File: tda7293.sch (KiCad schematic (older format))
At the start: 56 parts, among them J1 Screw_Terminal_01x04, J2 Screw_Terminal_01x04, J3 Screw_Terminal_01x02, J4 Screw_Terminal_01x03, Q1 BSS84, Q2 2N7002, U1 TDA7293, U2 TDA7293, U3 PC817, U4 MCP1792

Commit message: C substitutions, status LEDs, layout polishing
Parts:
- removed C1, C7: 22u, Capacitors_SMD:CP_Elec_6.3x7.7, symbol Device:CP
- removed C11, C5: 22u, Capacitors_ThroughHole:CP_Radial_D5.0mm_P2.00mm, symbol Device:CP
- added C1, C11, C24, C25, C5, C7: 10u, Capacitors_SMD:C_1206, symbol Device:C
- added D2, D3, D4: LED, LEDs:LED_0805, symbol Device:LED
- added R14: 1k, Resistors_SMD:R_0805, symbol Device:R
- added R15, R16: 10k, Resistors_SMD:R_0805, symbol Device:R
- C10, C4: footprint Capacitors_SMD:CP_Elec_6.3x7.7 -> Capacitors_ThroughHole:CP_Radial_D8.0mm_P3.50mm
- C2, C8: value 22u -> 22u NP; footprint Capacitors_ThroughHole:CP_Radial_D5.0mm_P2.00mm -> Capacitors_ThroughHole:CP_Radial_D8.0mm_P3.50mm; symbol Device:CP -> Device:C
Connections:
- wire segments 200 -> 229
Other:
- note added: "alt MCP1799"
- moved on the sheet: C10, C14, C15, C16, C17, C18, C19, C20, C21, C22, C23, C3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

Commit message: polishing, plotted output, added README
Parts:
- removed JP3: Jumper_NO_Small, Pin_Headers:Pin_Header_Straight_1x02_Pitch2.00mm, symbol Device:Jumper_NO_Small
- added R17, R18: 27k, Resistors_SMD:R_0805, symbol Device:R
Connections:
- wire segments 229 -> 231
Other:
- note added: "alt footprints\nfor MLCC or\nelectrolytic"
- note removed: "Alt Footprints\nfor 22u/50V\nelectrolytics"
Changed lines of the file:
@@
 	-1   0    0    1
 $EndComp
-Text Label 2500 3200 0    50   ~ 0
-5V
 $Comp
 L Device:R R11
@@
 $EndComp
 Wire Wire Line
-	2750 3800 2750 3850
-Wire Wire Line
 	2750 4000 2850 4000
 $Comp
@@
 Connection ~ 2250 7100
 Wire Wire Line
-	3000 6100 3800 6100
+	3000 6100 3300 6100
 Connection ~ 3000 6100
 Wire Wire Line
-	3000 6600 3800 6600
+	3000 6600 3300 6600
 $Comp
 L wbt-device:TDA7293 U1
@@
 Wire Wire Line
 	8100 2200 8300 2200
-Text Notes 5200 1450 0    50   ~ 0
-Alt Footprints\nfor 22u/50V\nelectrolytics
 Wire Wire Line
 	9200 2100 9200 2200
@@
 	9200 4350 9200 4500
 Connection ~ 8300 4500
-Text Notes 8250 3850 0    50   ~ 0
+Text Notes 8950 1950 0    50   ~ 0
 Close jumpers\nfor TDA7294
 Wire Wire Line
@@
 Wire Wire Line
 	6350 4200 6350 4300
-$Comp
-L Device:Jumper_NO_Small JP3
-U 1 1 61F9C8CB
-P 2250 3000
-F 0 "JP3" H 2250 2815 50  0000 C CNN
-F 1 "Jumper_NO_Small" H 2250 2906 50  0000 C CNN
-F 2 "Pin_Headers:Pin_Header_Straight_1x02_Pitch2.00mm" H 2250 3000 50  0001 C CNN
-F 3 "~" H 2250 3000 50  0001 C CNN
-	1    2250 3000
-	-1   0    0    1
-$EndComp
 Text Notes 3100 3600 0    50   ~ 0
 or AO3401 etc
-Wire Wire Line
-	2350 3000 2850 3000
-Wire Wire Line
-	2150 3000 1800 3000
-Text Label 1850 3000 0    50   ~ 0
-VCC
 Wire Wire Line
 	2000 4650 2050 4650
@@
 	2050 4000 2050 3950
 Wire Wire Line
-	2750 3850 2850 3850
-Wire Wire Line
-	2850 3850 2850 3000
-Connection ~ 2750 3850
-Wire Wire Line
-	2750 3850 2750 4000
-Wire Wire Line
 	2050 3650 2050 3200
 Wire Wire Line
@@
 Wire Wire Line
 	1300 6550 1300 6600
+Text Label 2500 3200 0    50   ~ 0
+5V
+Wire Wire Line
+	2750 3800 2750 4000
+Text Notes 8100 2000 0    50   ~ 0
+alt footprints\nfor MLCC or\nelectrolytic
+$Comp
+L Device:R R17
+U 1 1 61D28AD4
+P 3300 6350
+F 0 "R17" V 3093 6350 50  0000 C CNN
+F 1 "27k" V 3184 6350 50  0000 C CNN
+F 2 "Resistors_SMD:R_0805" V 3230 6350 50  0001 C CNN
+F 3 "~" H 3300 6350 50  0001 C CNN
+	1    3300 6350
+	-1   0    0    1
+$EndComp
+$Comp
+L Device:R R18
+U 1 1 61D38B3B
+P 3300 6850
+F 0 "R18" V 3093 6850 50  0000 C CNN
+F 1 "27k" V 3184 6850 50  0000 C CNN
+F 2 "Resistors_SMD:R_0805" V 3230 6850 50  0001 C CNN
+F 3 "~" H 3300 6850 50  0001 C CNN
+	1    3300 6850
+	-1   0    0    1
+$EndComp
+Wire Wire Line
+	3300 6500 3300 6600
+Connection ~ 3300 6600
+Wire Wire Line
+	3300 6600 3800 6600
+Wire Wire Line
+	3300 6600 3300 6700
+Wire Wire Line
+	3300 7000 3300 7100
+Wire Wire Line
+	3300 7100 3000 7100
+Connection ~ 3000 7100
+Wire Wire Line
+	3300 6100 3300 6200
+Connection ~ 3300 6100
+Wire Wire Line
+	3300 6100 3800 6100
 $EndSCHEMATC

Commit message: removed holes, moved input filters, fancier unmute timing per datasheet
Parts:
- removed H3, H4: MountingHole, Mounting_Holes:MountingHole_3.2mm_M3, symbol Mechanical:MountingHole
- added C26: 10u, Capacitors_SMD:C_0805, symbol Device:C
- added D5: LL4148, Diodes_SMD:D_MiniMELF, symbol Device:D
- added R19: 27k, Resistors_SMD:R_0805, symbol Device:R
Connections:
- net labels added: STBY
- wire segments 231 -> 230
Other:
- note added: "alt AO3401"
- note removed: "Close jumpers\nfor TDA7294"
- note removed: "Delete Q1, Q2, U4\nand close jumper\nfor auto-unmute"
- note removed: "or AO3401 etc"
- moved on the sheet: C13, C14, C15, C16, C17, C18, C19, C20, C21, C22, C23, C3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

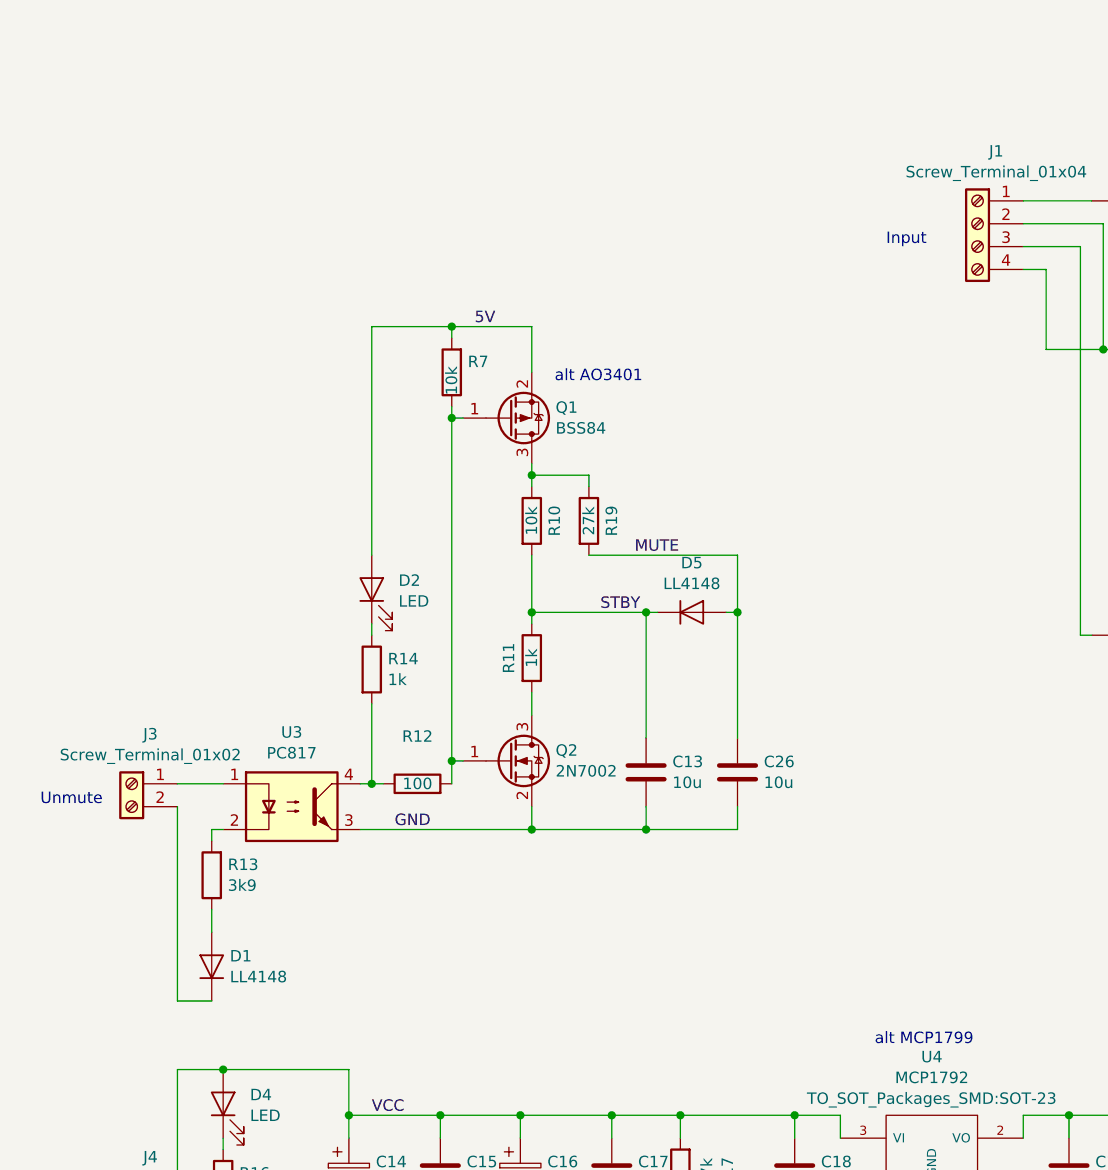
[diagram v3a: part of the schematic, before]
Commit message: moved a resistor, plotted ready for manufacture
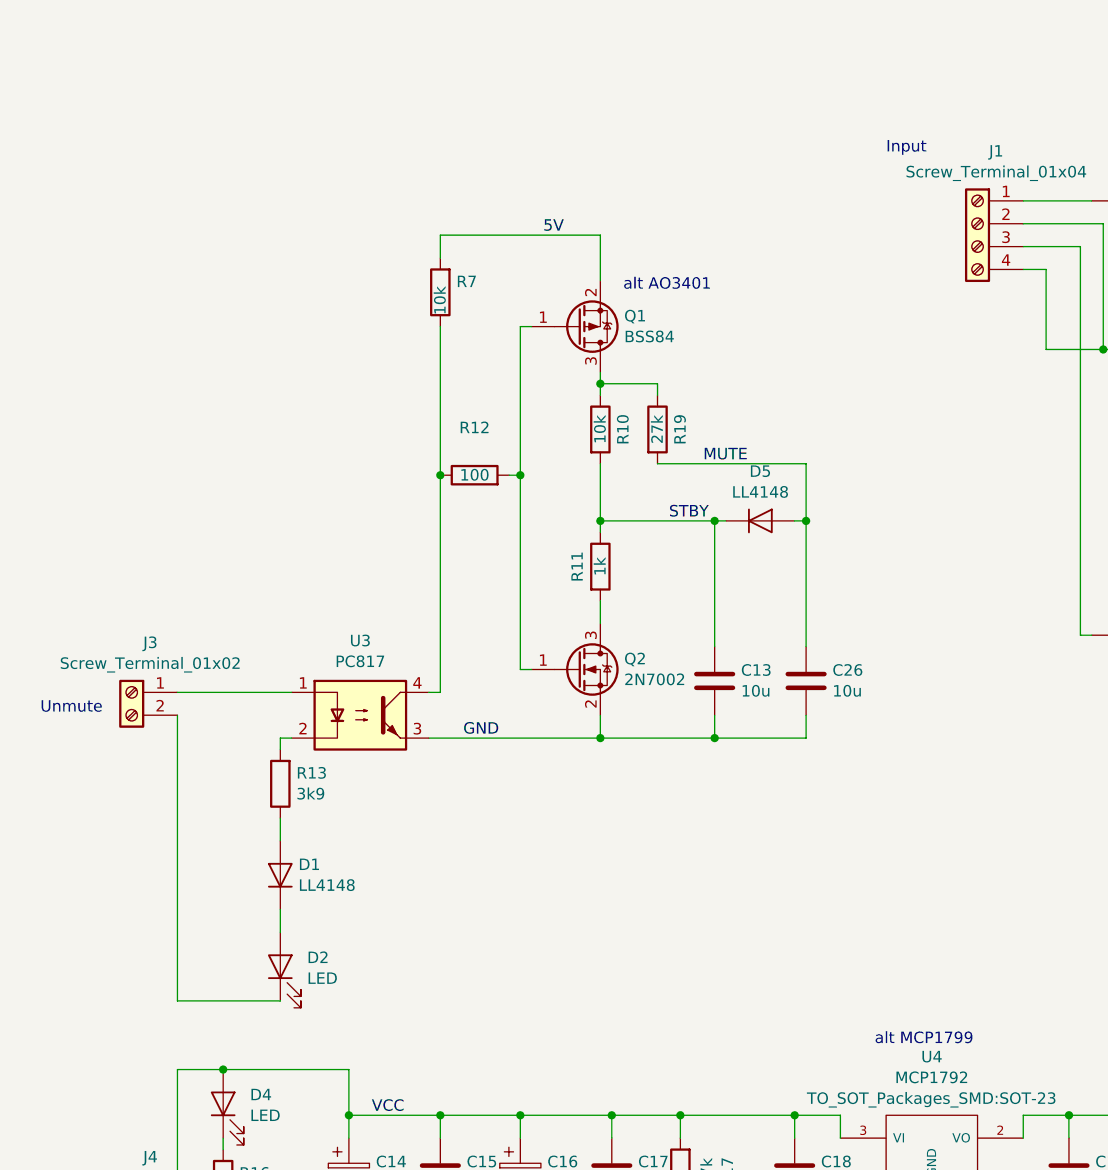
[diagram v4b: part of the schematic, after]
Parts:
- removed R14: 1k, Resistors_SMD:R_0805, symbol Device:R
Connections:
- wire segments 230 -> 228
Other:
- moved on the sheet: C13, C26, D1, D2, D5, J3, Q1, Q2, R10, R11, R12, R13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

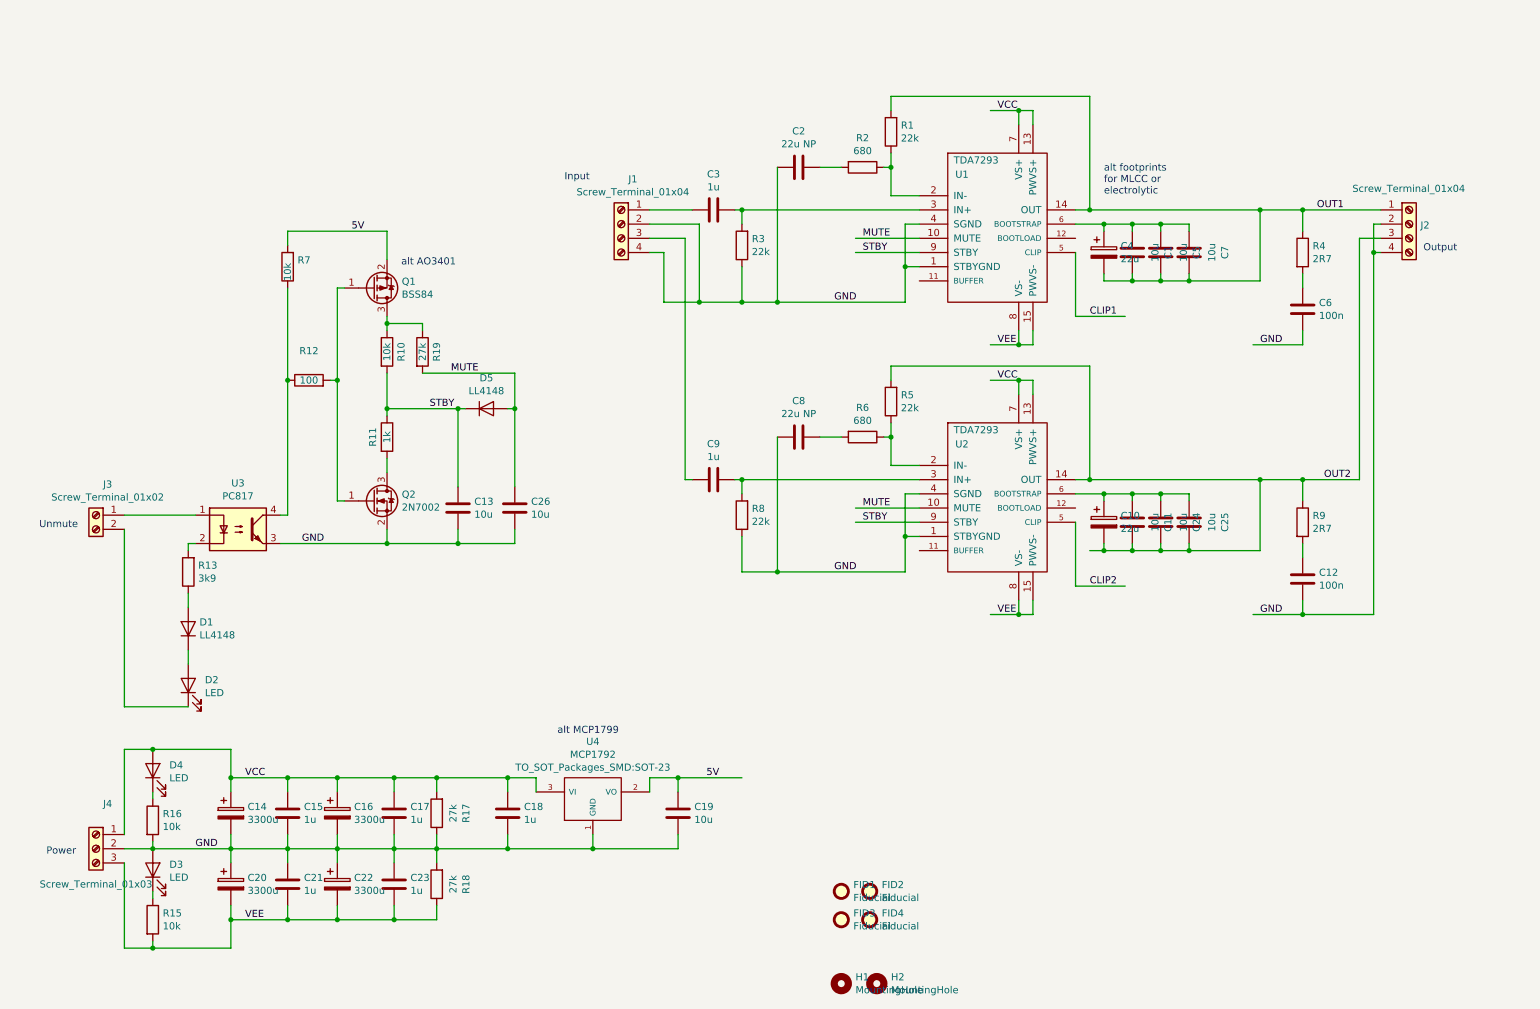
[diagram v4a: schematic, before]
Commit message: Redrafted as Rev.B: hum-break resistors, better GND topology, fuses, room for heatsink screwdrivers!
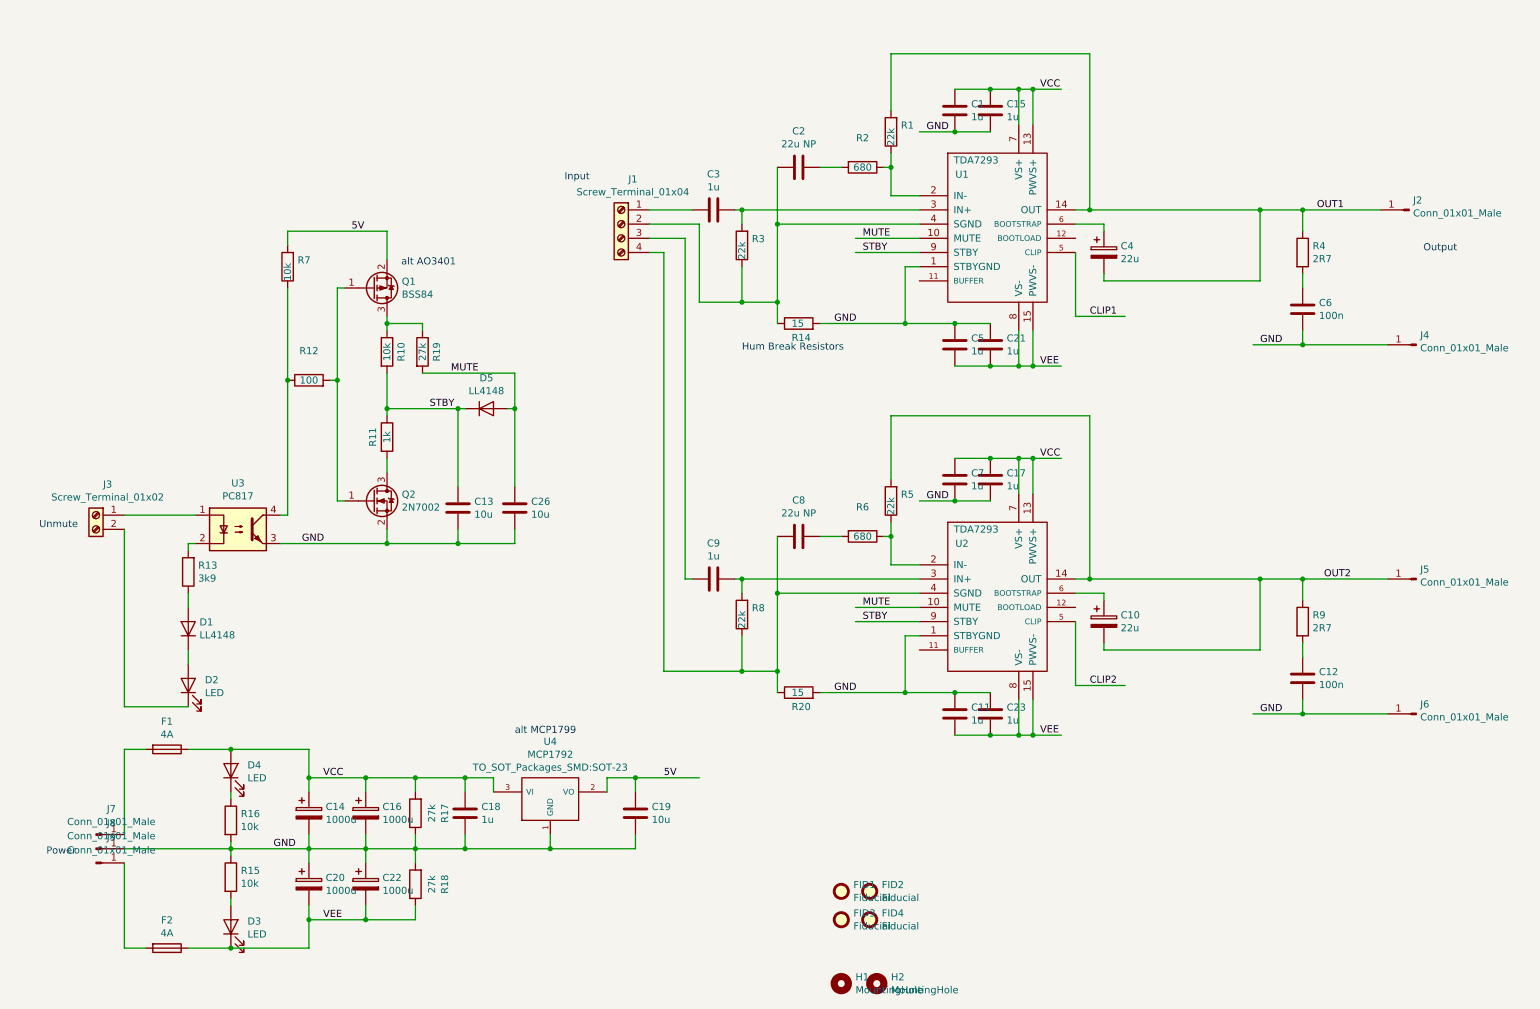
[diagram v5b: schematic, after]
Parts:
- removed C24, C25: 10u, Capacitors_SMD:C_1206, symbol Device:C
- removed J2: Screw_Terminal_01x04, Terminals_Phoenix:TerminalBlock_Phoenix_MKDS1.5-4pol, symbol Connector:Screw_Terminal_01x04
- removed J4: Screw_Terminal_01x03, Terminals_Phoenix:TerminalBlock_Phoenix_MKDS1.5-3pol, symbol Connector:Screw_Terminal_01x03
- added F1, F2: 4A, power:Fuseholder5x20_6mm, symbol Device:Fuse
- added J2, J4, J5, J6, J7, J8, J9: Conn_01x01_Male, power:FASTON250P_5.08mm_male_vertical, symbol Connector:Conn_01x01_Male
- added R14, R20: 15, Resistors_SMD:R_0805, symbol Device:R
- C1, C11, C5, C7: value 10u -> 1u; footprint Capacitors_SMD:C_1206 -> Capacitors_SMD:C_0805
- C14, C16, C20, C22: value 3300u -> 1000u; footprint Capacitors_ThroughHole:CP_Radial_D18.0mm_P7.50mm -> Capacitors_ThroughHole:CP_Radial_D16.0mm_P7.50mm
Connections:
- wire segments 228 -> 204
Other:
- note added: "Hum Break Resistors"
- note removed: "alt footprints\nfor MLCC or\nelectrolytic"
- moved on the sheet: C10, C12, C14, C15, C16, C17, C18, C19, C20, C21, C22, C23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

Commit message: silk-screen updates, turd-polishing, plotted gerbers
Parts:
- removed C1, C11, C5, C7: 1u, Capacitors_SMD:C_0805, symbol Device:C
- removed D3, D4: LED, LEDs:LED_0805, symbol Device:LED
- removed J1: Screw_Terminal_01x04, Terminals_Phoenix:TerminalBlock_Phoenix_MPT-2.54mm_4pol, symbol Connector:Screw_Terminal_01x04
- removed R15, R16: 10k, Resistors_SMD:R_0805, symbol Device:R
- added H3, H4: MountingHole, Mounting_Holes:MountingHole_3.2mm_M3, symbol Mechanical:MountingHole
- added J1, J6: Screw_Terminal_01x02, Terminals_Phoenix:TerminalBlock_Phoenix_MPT-2.54mm_2pol, symbol Connector:Screw_Terminal_01x02
- added J11, J5: Conn_01x01_Male, power:FASTON250P_5.08mm_male_vertical, symbol Connector:Conn_01x01_Male
- added R18, R8: 0R, Resistors_SMD:R_0805, symbol Device:R
- added R21, R22: 27k, Resistors_SMD:R_0805, symbol Device:R
- added R23: 1k, Resistors_SMD:R_0805, symbol Device:R
- C11: renamed from C10; footprint Capacitors_ThroughHole:CP_Radial_D8.0mm_P3.50mm -> Capacitors_ThroughHole:CP_Radial_D6.3mm_P2.50mm
- C5: renamed from C4; footprint Capacitors_ThroughHole:CP_Radial_D8.0mm_P3.50mm -> Capacitors_ThroughHole:CP_Radial_D6.3mm_P2.50mm
- R17: renamed from R20; value 15 -> 10
- R7: renamed from R14; value 15 -> 10
- renumbered C18 to C1, C9 to C10, C14 to C13, C15 to C14, C16 to C15, C17 to C16, C20 to C17, C21 to C18, C22 to C19, C19 to C2, C23 to C20, C2 to C3, C3 to C4, C13 to C7, C26 to C8, C8 to C9, D5 to D1, D1 to D2, D2 to D3, J8 to J10, J9 to J12, J5 to J7, J6 to J8, J7 to J9, R19 to R10, R13 to R11, R11 to R12, R5 to R13, R6 to R14, R8 to R15, R9 to R16, R17 to R19, R18 to R20, R7 to R4, R4 to R5, R12 to R6, R10 to R9, U4 to U1, U1 to U2, U2 to U4
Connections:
- net labels added: LGND, OUTL, OUTR, RGND, SGND
- net labels removed: GND, OUT1, OUT2
- wire segments 204 -> 203
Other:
- note removed: "Hum Break Resistors"
- note removed: "Input"
- note removed: "Output"
- moved on the sheet: C1, C11, C12, C13, C14, C15, C16, C17, C18, C19, C2, C20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
